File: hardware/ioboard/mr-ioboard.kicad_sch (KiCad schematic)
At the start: 43 parts

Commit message: Working on debug/IO board
Signed-off-by: gatecat <gatecat@ds0.me>
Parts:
- removed C?: 10µ, symbol Device:C_Small
- added C?: 1µ, symbol Device:C_Small
- added C? (x5): 470n, symbol Device:C_Small
- added C? (x9): 10µ, Capacitor_SMD:C_0805_2012Metric, symbol Device:C_Small
- added C? (x2): 1u, symbol Device:C_Small
- added C?: 22µ, symbol Device:C_Polarized_Small
- added C?: 10n, Capacitor_SMD:C_0805_2012Metric, symbol Device:C_Small
- added C? (x3): 10µ, symbol Device:C_Small
- added D? (x3): LED_Small, symbol Device:LED_Small
- added J?: Micro_SD_Card_Det, symbol Connector:Micro_SD_Card_Det
- added J?: Conn_01x40_Shielded, meowality:TE_FPC_40pin_p0.5mm_4-1734839-0, symbol Connector_Generic_Shielded:Conn_01x40_Shielded
- added L? (x2): XFL4015-471MEB, Inductor_SMD:L_Coilcraft_XxL4020, symbol Device:L_Small
- added R? (x6): 10k, symbol Device:R_Small
- added R? (x4): 10k, Resistor_SMD:R_0402_1005Metric, symbol Device:R_Small
- added R? (x2): 200k, symbol Device:R_Small
- added R? (x3): 2.2k, symbol Device:R_Small
- added R?: 8.45k, Resistor_SMD:R_0402_1005Metric, symbol Device:R_Small
- added R?: 15k, Resistor_SMD:R_0402_1005Metric, symbol Device:R_Small
- added SW?: SW_Push, symbol Switch:SW_Push
- added U?: LD3985M28R_SOT23, Package_TO_SOT_SMD:SOT-23-5, symbol Regulator_Linear:LD3985M28R_SOT23
- added U?: DS90C363, symbol meowality:DS90C363
- added U? (x2): TPS62822, meowality:TI_VSON-HR_1.5x2mm_p0.5mm, symbol meowality:TPS62823
- C? (x4): value 4.7µ -> 10µ
- C? (x2): value 10µ -> 10µ/25V
- C?: value 470n -> 1µ
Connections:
- net +1V1: now also C?.1, C?.1, L?.2, R?.1
- net +2V8: now also C?.1, U?.5 (VOUT)
- net +3V3: now also C?.1, C?.1, C?.1, C?.1, C?.1, C?.1, C?.1, C?.1, C?.1, J?.1 (Pin_1), J?.2 (Pin_2), J?.3 (Pin_3), J?.4 (Pin_4), J?.4 (VDD), R?.1, R?.1, R?.1, R?.1, R?.1, R?.1, R?.2, R?.2, U?.1 (EN), U?.1 (EN), U?.1 (VIN), U?.2 (Vcc), U?.21 (Vcc), U?.29 (PLL_Vcc), U?.3 (INH), U?.37 (LVDS_Vcc), U?.7 (Vin), U?.7 (Vin), U?.8 (Vcc)
- net FPGA_AUX0: now also J?.10 (Pin_10)
- net FPGA_AUX1: now also J?.9 (Pin_9)
- net FPGA_AUX2: now also J?.8 (Pin_8)
- net FPGA_JTAG_TCK: now also J?.14 (Pin_14)
- net FPGA_JTAG_TDI: now also J?.13 (Pin_13)
- net FPGA_JTAG_TDO: now also J?.12 (Pin_12)
- net FPGA_JTAG_TMS: now also J?.15 (Pin_15)
- net GND: now also C?.2, C?.2, C?.2, C?.2, C?.2, C?.2, C?.2, C?.2, C?.2, C?.2, C?.2, C?.2, C?.2, C?.2, C?.2, C?.2, C?.2, C?.2, C?.2, C?.2, D?.1 (K), D?.1 (K), D?.1 (K), J?.11 (Pin_11), J?.11 (SHIELD), J?.16 (Pin_16), J?.19 (Pin_19), J?.22 (Pin_22), J?.25 (Pin_25), J?.28 (Pin_28), J?.31 (Pin_31), J?.34 (Pin_34), J?.37 (Pin_37), J?.40 (Pin_40), J?.6 (Pin_6), J?.6 (VSS), J?.7 (Pin_7), J?.9 (DET_B), J?.SH (Shield), R?.2, R?.2, R?.2, R?.2, SW?.1, U?.11 (GND), U?.17 (GND), U?.2 (GND), U?.24 (GND), U?.28 (PLL_GND), U?.3 (AGND), U?.3 (AGND), U?.30 (PLL_GND), U?.31 (LVDS_GND), U?.36 (LVDS_GND), U?.42 (LVDS_GND), U?.46 (GND), U?.5 (GND), U?.5 (PGND), U?.5 (PGND)
- net LCD_CLK: now also U?.26 (TxCKIN)
- net LCD_D10: now also U?.4 (TxIN6)
- net LCD_D11: now also U?.6 (TxIN7)
- net LCD_D12: now also U?.7 (TxIN8)
- net LCD_D13: now also U?.9 (TxIN9)
- net LCD_D14: now also U?.10 (TxIN10)
- net LCD_D15: now also U?.12 (TxIN11)
- net LCD_D18: now also U?.13 (TxIN12)
- net LCD_D19: now also U?.15 (TxIN13)
- net LCD_D2: now also U?.44 (TxIN0)
- net LCD_D20: now also U?.16 (TxIN14)
- net LCD_D21: now also U?.18 (TxIN15)
- net LCD_D22: now also U?.19 (TxIN16)
- net LCD_D23: now also U?.20 (TxIN17)
- net LCD_D3: now also U?.45 (TxIN1)
- net LCD_D4: now also U?.47 (TxIN2)
- net LCD_D5: now also U?.48 (TxIN3)
- net LCD_D6: now also U?.1 (TxIN4)
- net LCD_D7: now also U?.3 (TxIN5)
- net LCD_DE: now also U?.25 (TxIN20/DEN)
- net LCD_HSYNC: now also U?.22 (TxIN18/HSYNC)
- net LCD_VSYNC: now also U?.23 (TxIN19/VSYNC)
- net LED0: now also U?.44 (PE5), R?.1; no longer U?.47 (PE2)
- net LED1: now also R?.1
- net LED2: now also R?.1
- net RESET: now also C?.1, R?.2, SW?.2
- net SDCARD_CLK: now also J?.5 (CLK)
- net SDCARD_CMD: now also J?.3 (CMD), R?.2
- net SDCARD_D0: now also J?.7 (DAT0)
- net SDCARD_D1: now also J?.8 (DAT1)
- net SDCARD_D2: now also J?.1 (DAT2)
- net SDCARD_D3: now also J?.2 (DAT3/CD), R?.2
- net SDCARD_DET: now also J?.10 (DET_A), R?.2
- net VBUS: now also C?.1
- net at C?.1, C?.1, FB?.1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: now also C?.1
- net at U?.75 (TV_Vrn): now also C?.1, C?.2
- net at U?.76 (TV_Vrp): now also C?.1, C?.2
- net Vra1: now reaches U?.81 (Vra1)
- net Vra1: now also C?.1, R?.1
- net Vra2: now reaches U?.83 (Vra2)
- net Vra2: now also C?.1, R?.1
- new net: L?.1, U?.6 (SW) (x2)
- new net: R?.2, U?.8 (PG) (x2)
- new net: R?.1, R?.2, U?.2 (FB) (x2)
- new net: C?.1, U?.4 (BYP)
- new net: R?.1, U?.14 (R_~F)
- new net: D?.2 (A), R?.2 (x3)
- new net: R?.1, U?.27 (~PWRDN)
- new net +1V5: C?.1, C?.1, L?.2, R?.1
- new net LVDS_CLK+: J?.33 (Pin_33), U?.32 (TxCKOUT+)
- new net LVDS_CLK-: J?.32 (Pin_32), U?.33 (TxCKOUT-)
- new net LVDS_D0+: J?.24 (Pin_24), U?.40 (TxOUT0+)
- new net LVDS_D0-: J?.23 (Pin_23), U?.41 (TxOUT0-)
- new net LVDS_D1+: J?.21 (Pin_21), U?.38 (TxOUT1+)
- new net LVDS_D1-: J?.20 (Pin_20), U?.39 (TxOUT1-)
- new net LVDS_D2+: J?.18 (Pin_18), U?.34 (TxOUT2+)
- new net LVDS_D2-: J?.17 (Pin_17), U?.35 (TxOUT2-)
- new net USB_ID: U?.47 (PE2)
- no-connect marks 4 -> 13
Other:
- note added: "Check JTAG and LVDS dir"
- note removed: "1.1V supply..."
- note removed: "1.5V supply..."
- note removed: "2.8V supply..."
- moved on the sheet: C?, J?, L?, R?, TP?, U?

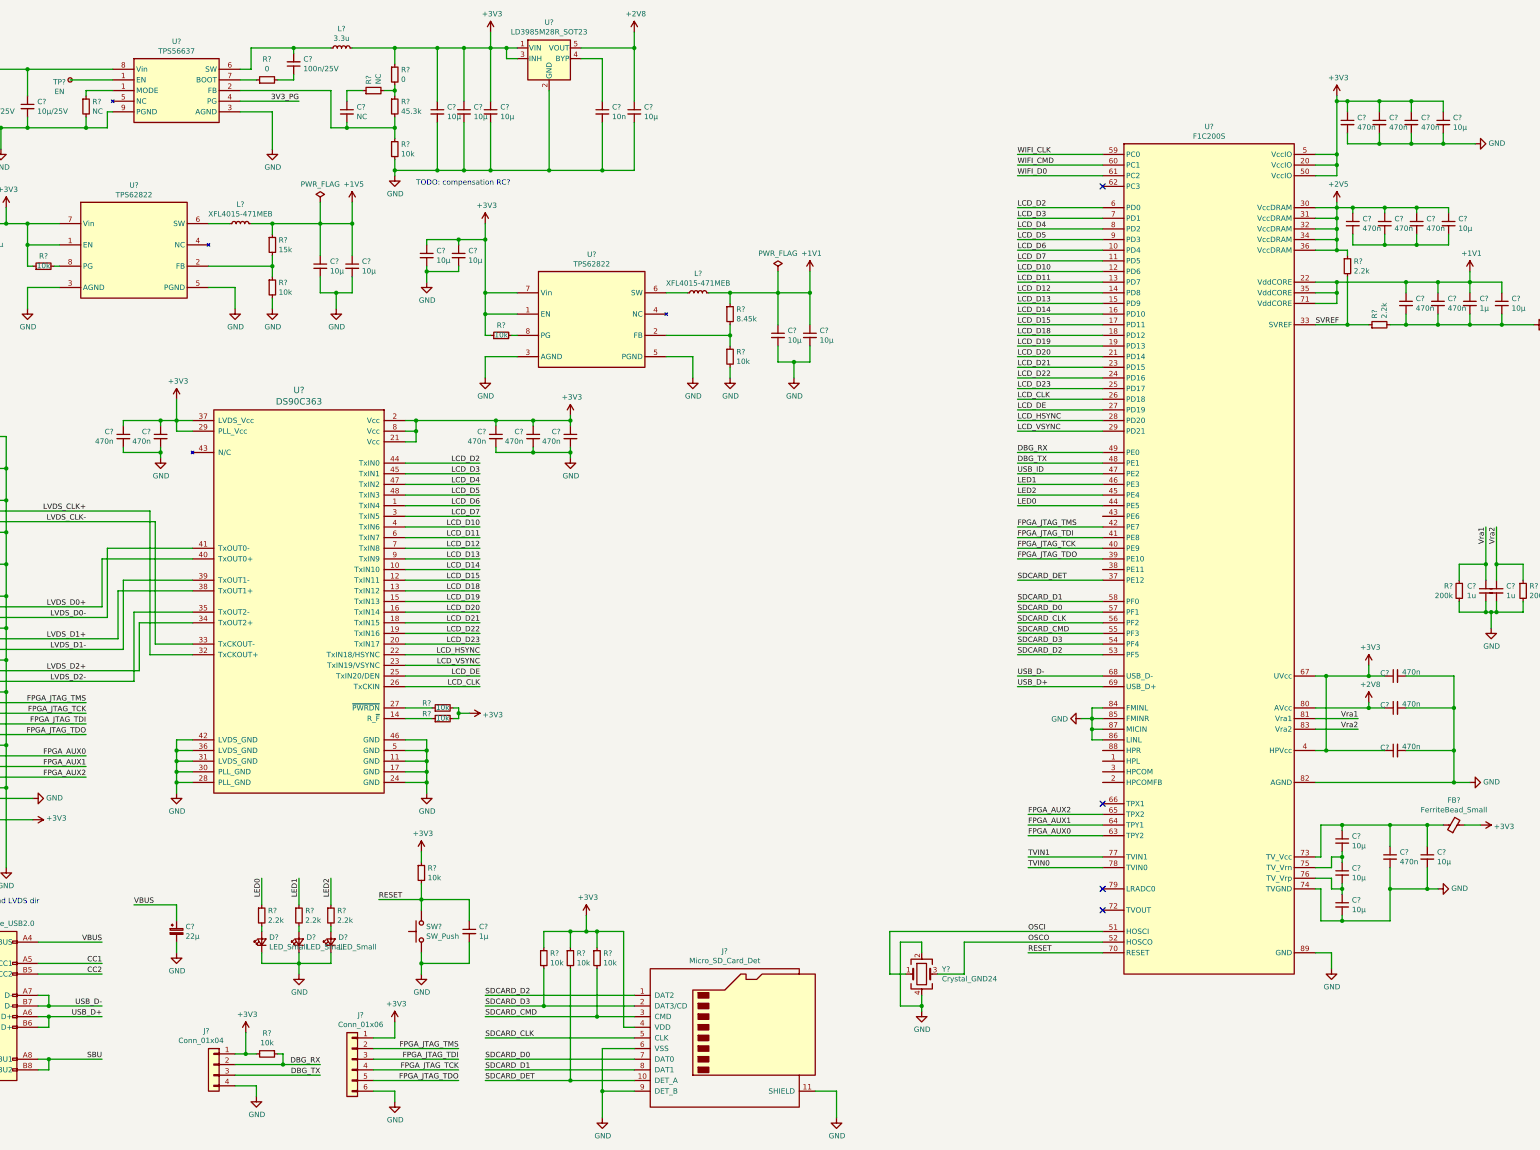
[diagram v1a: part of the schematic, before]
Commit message: Add USBC controller and ESD diodes
Signed-off-by: gatecat <gatecat@ds0.me>
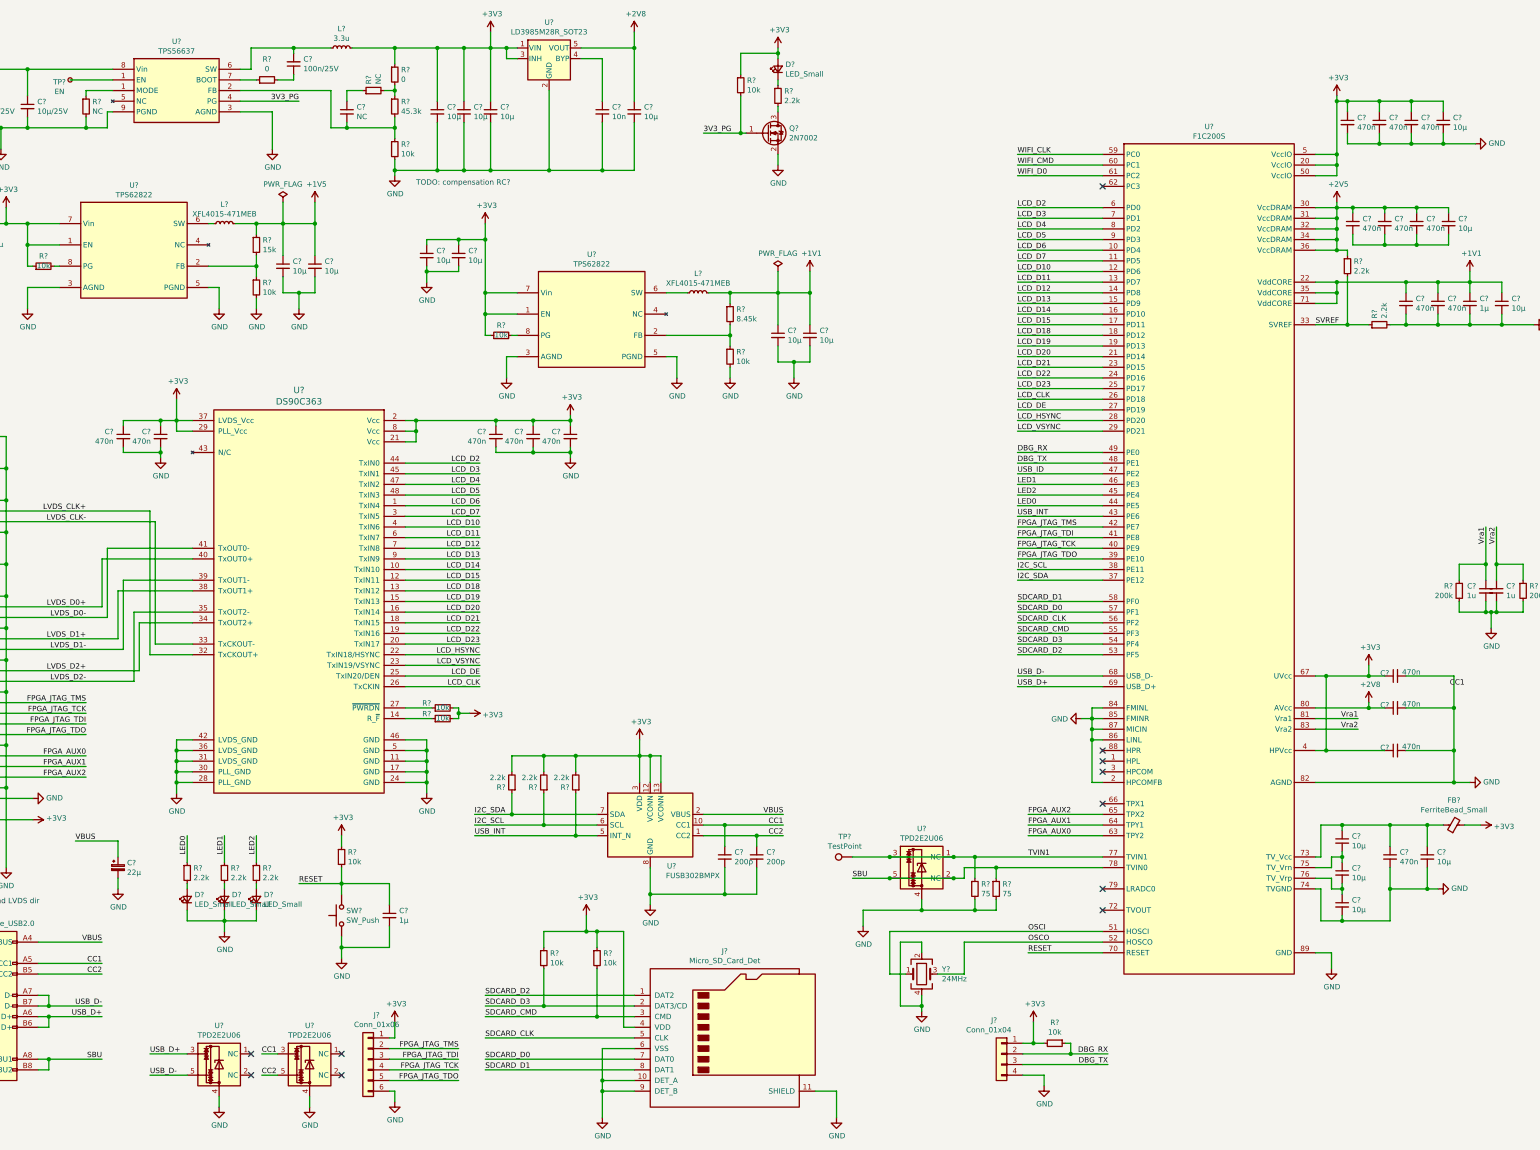
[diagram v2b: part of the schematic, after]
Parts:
- removed R?: 10k, symbol Device:R_Small
- added C? (x2): 200p, symbol Device:C_Small
- added D?: LED_Small, symbol Device:LED_Small
- added Q?: 2N7002, Package_TO_SOT_SMD:SOT-23, symbol Transistor_FET:2N7002
- added R? (x2): 75, symbol Device:R_Small
- added R? (x4): 2.2k, symbol Device:R_Small
- added R?: 10k, symbol Device:R_Small
- added TP?: TestPoint, symbol Connector:TestPoint
- added U? (x3): TPD2E2U06, Package_TO_SOT_SMD:SOT-543, symbol Power_Protection:TPD2E2U06
- added U?: FUSB302BMPX, Package_DFN_QFN:WQFN-14-1EP_2.5x2.5mm_P0.5mm_EP1.45x1.45mm, symbol Interface_USB:FUSB302BMPX
- Y?: value Crystal_GND24 -> 24MHz
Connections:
- net TVIN0 is gone; now on net SBU: U?.78 (TVIN0)
- net +3V3: now also D?.2 (A), R?.1, R?.2, R?.2, R?.2, U?.12 (VCONN), U?.13 (VCONN), U?.3 (VDD), U?.4 (VDD)
- net 3V3_PG: now also Q?.1 (G), R?.2
- net CC1: now also C?.1, U?.10 (CC1), U?.11 (CC1), U?.3
- net CC2: now also C?.1, U?.1 (CC2), U?.14 (CC2), U?.5
- net GND: now also J?.10 (DET_A), U?.2 (HPCOMFB), C?.2, C?.2, Q?.2 (S), R?.2, R?.2, U?.15 (GND), U?.4, U?.4, U?.4, U?.8 (GND), U?.9 (GND)
- net SBU: now also R?.1, U?.2 (NC), U?.5
- net TVIN1: now also R?.1, TP?.1, U?.1 (NC), U?.3
- net USB_D+: now also U?.3
- net USB_D-: now also U?.5
- net VBUS: now also U?.2 (VBUS)
- net I2C_SCL: now reaches U?.38 (PE11)
- net I2C_SCL: now also R?.1, U?.6 (SCL)
- net USB_INT: now reaches U?.43 (PE6)
- net USB_INT: now also R?.1, U?.5 (INT_N)
- net SDCARD_DET renamed I2C_SDA
- net I2C_SDA: now also R?.1, U?.7 (SDA); no longer J?.10 (DET_A)
- new net: D?.1 (K), R?.1
- new net: Q?.3 (D), R?.2
- no-connect marks 13 -> 20
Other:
- moved on the sheet: C?, D?, J?, L?, R?, SW?
